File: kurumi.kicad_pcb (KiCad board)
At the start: 2 copper layers, 36 x 30 mm, 21 parts, among them J1 Power input, J2 LEDs, J3 Ext MOSFET/relay, U1 ESP32-C3_SUPERMINI, U2 SN74LVC1T45DRL, U3 TPS54308

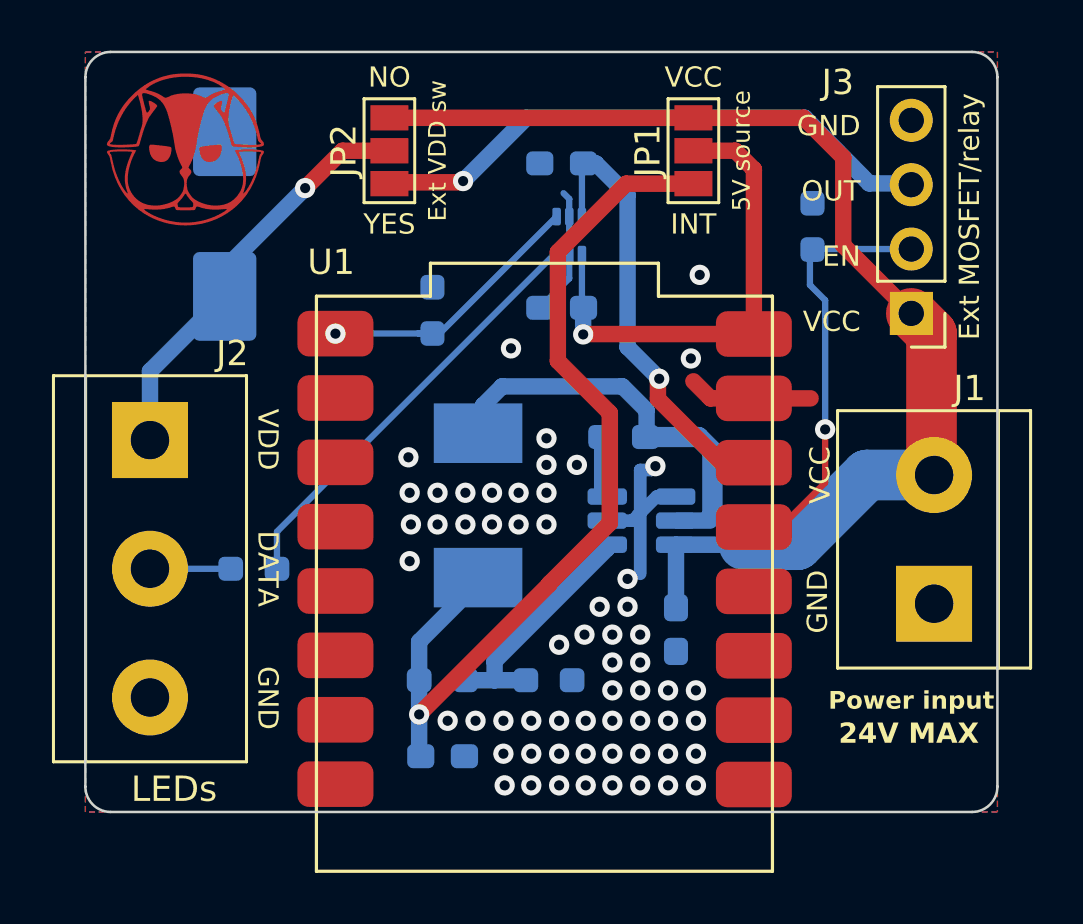
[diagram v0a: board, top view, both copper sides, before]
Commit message: Parts updates, BOM and CPL
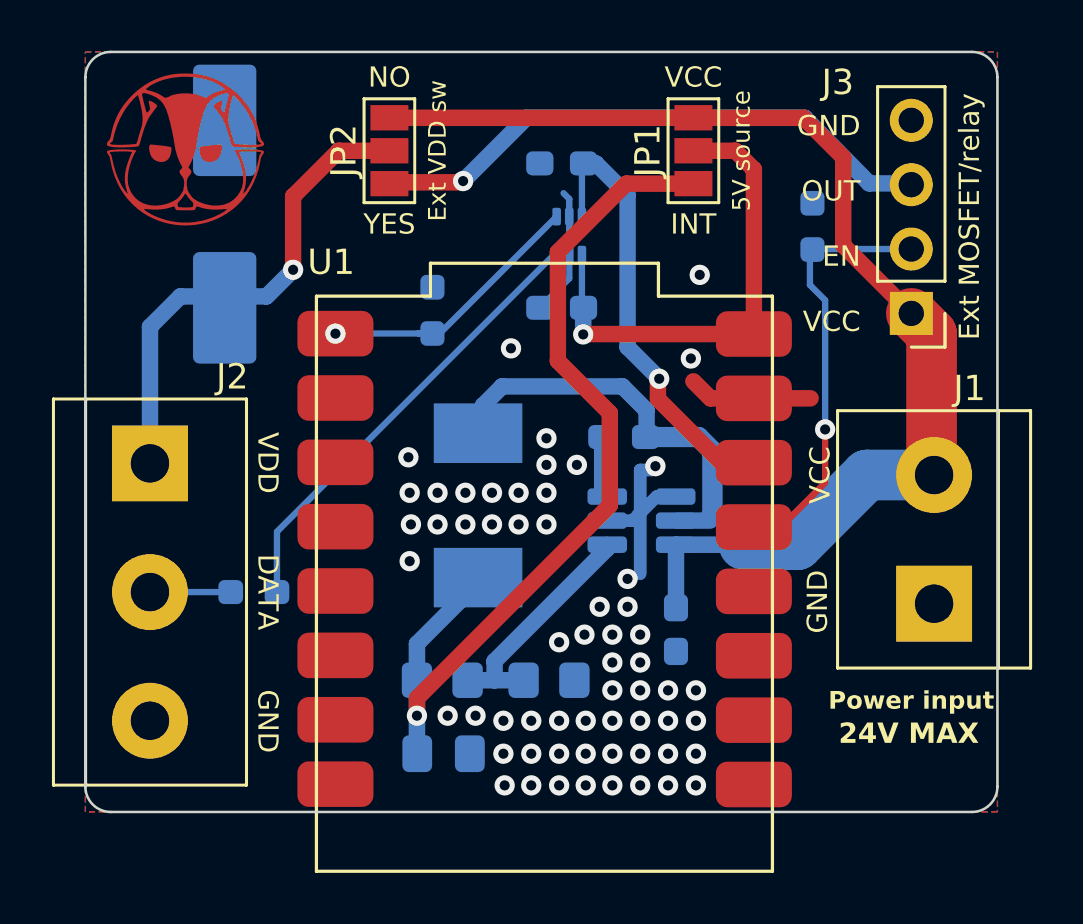
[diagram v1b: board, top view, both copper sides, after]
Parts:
- C5: footprint Capacitor_SMD:C_0603_1608Metric_Pad1.08x0.95mm_HandSolder -> Capacitor_SMD:C_0805_2012Metric_Pad1.18x1.45mm_HandSolder
- C6: footprint Capacitor_SMD:CP_Elec_8x10 -> Capacitor_SMD:CP_Elec_8x10.5
- R4: value 100k -> 100K; footprint Resistor_SMD:R_0603_1608Metric_Pad0.98x0.95mm_HandSolder -> Resistor_SMD:R_0805_2012Metric_Pad1.20x1.40mm_HandSolder
- R5: value 13.7k -> 13.7K; footprint Resistor_SMD:R_0603_1608Metric_Pad0.98x0.95mm_HandSolder -> Resistor_SMD:R_0805_2012Metric_Pad1.20x1.40mm_HandSolder
- moved R1 0.92 mm to (20.2, 33.4)
- moved J2 0.92 mm to (16.1, 28.3)
- moved C5 0.11 mm to (27.7, 39.8)
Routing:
- net VDD: track 16.4 -> 18.5 mm
- net Net-(U2-A): track 17.0 -> 18.0 mm
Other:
- board text removed: "LEDs"

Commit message: Minor changes
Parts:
- moved C4 0.95 mm to (35.8, 27.3)
- moved U3 0.45 mm to (35.1, 30.6)
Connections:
- U3 pad 5: GND -> unconnected-(U3-EN-Pad5)
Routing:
- net GND: track 19.3 -> 0.00 mm, vias 60 -> 75
- net +3.3V: track 17.8 -> 22.5 mm
- net V_OUT: track 37.0 -> 35.1 mm
- net VDD_EN: track 16.9 -> 18.8 mm
- net Net-(U3-BOOT): track 2.44 -> 3.15 mm
- net +5V: track 19.1 -> 18.5 mm
- net Net-(U3-SW): track 16.1 -> 15.4 mm, vias 0 -> 2

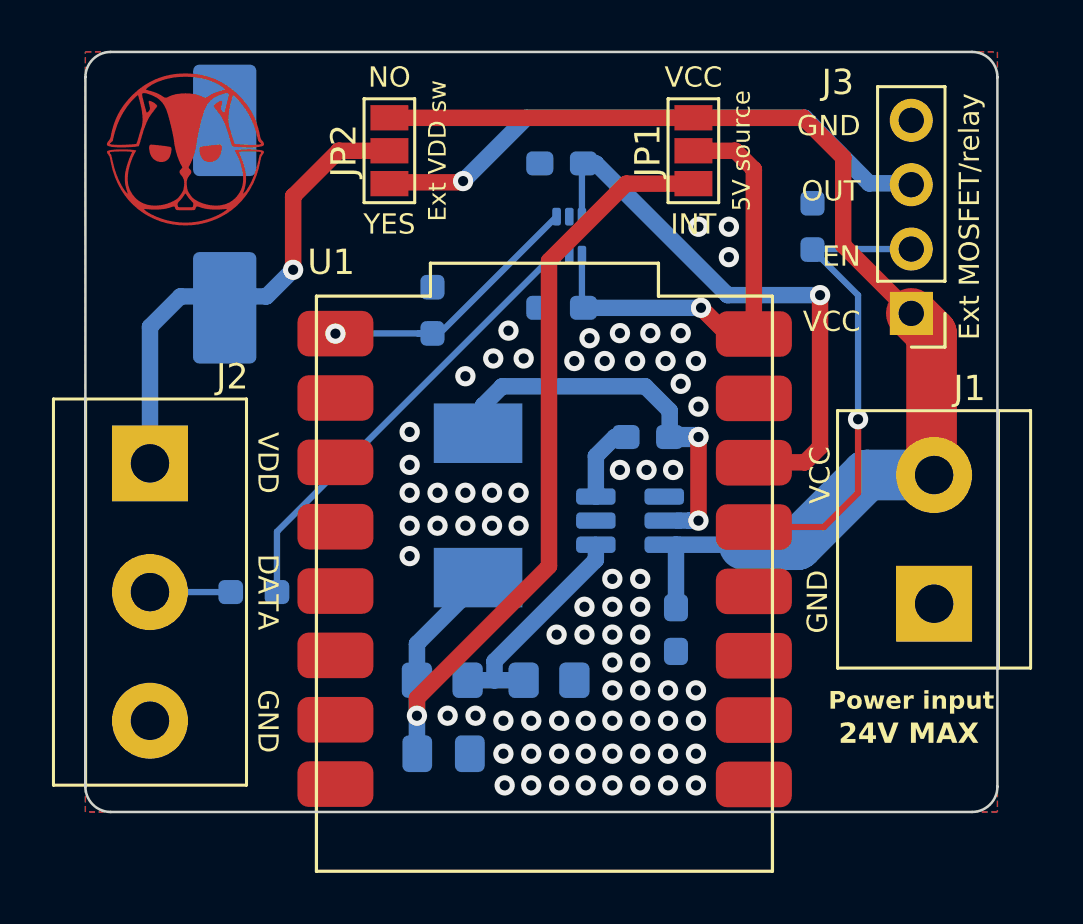
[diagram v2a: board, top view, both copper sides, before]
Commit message: Addes USB slot, fixed libraries
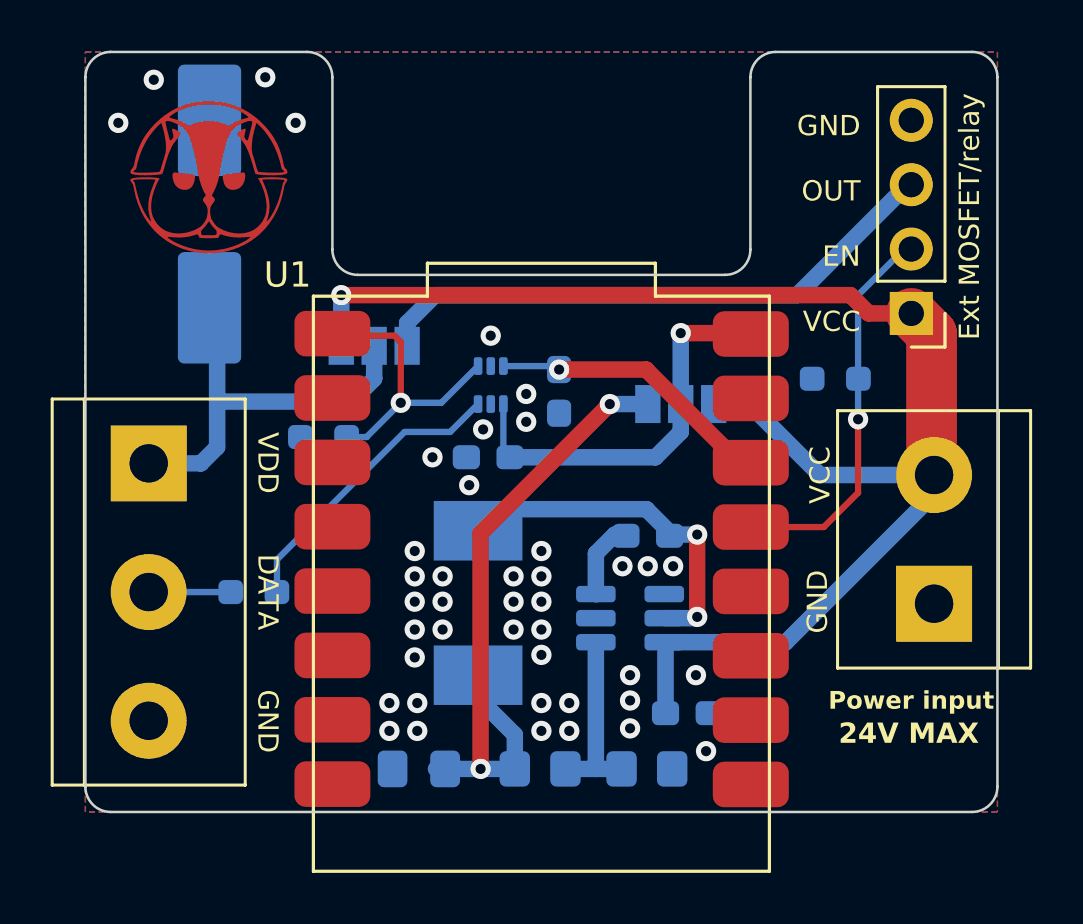
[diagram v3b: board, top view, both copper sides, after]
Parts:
- JP1, JP2: moved to B.Cu
- moved JP1 10.0 mm to (37.1, 26.0), turned to 0 degrees
- moved C2 9.00 mm to (32.3, 25.5), turned to 90 degrees
- moved JP2 7.72 mm to (25.0, 23.7), turned to 0 degrees
- moved U2 6.66 mm to (29.6, 25.2)
- moved R2 6.59 mm to (23.0, 27.3), turned to 180 degrees
- moved C1 6.57 mm to (29.5, 28.1)
- moved R3 6.08 mm to (43.2, 25.0), turned to 180 degrees
- moved R5 5.21 mm to (35.8, 40.4)
- moved R4 5.21 mm to (31.6, 40.4)
- moved C4 3.90 mm to (35.8, 31.2)
- moved L1 3.85 mm to (29.1, 33.9)
- moved U3 3.85 mm to (35.1, 34.5)
- moved C3 3.33 mm to (37.4, 38.2), turned to 0 degrees
- moved REF** 1.44 mm to (15.3, 14.0)
- moved C5 1.14 mm to (26.8, 40.4), turned to 180 degrees
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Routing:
- net VCC: track 45.0 -> 57.9 mm, vias 0 -> 1
- net +3.3V: track 22.5 -> 11.3 mm
- net V_OUT: track 35.1 -> 25.4 mm, vias 1 -> 2
- net Net-(U2-A): track 18.0 -> 11.8 mm
- net VDD_EN: track 18.8 -> 15.3 mm
- net +5V: track 18.5 -> 15.8 mm
- net Net-(U3-FB): track 9.39 -> 7.22 mm
- net Net-(U3-SW): track 15.4 -> 14.2 mm
- net VDD: track 18.5 -> 17.4 mm, vias 1 -> 0
- net V_SW: track 22.8 -> 22.5 mm, vias 1 -> 0
- net GND: vias 75 -> 42
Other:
- outline, holes or cut-outs redrawn

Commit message: Buck converter fix by @CRImier
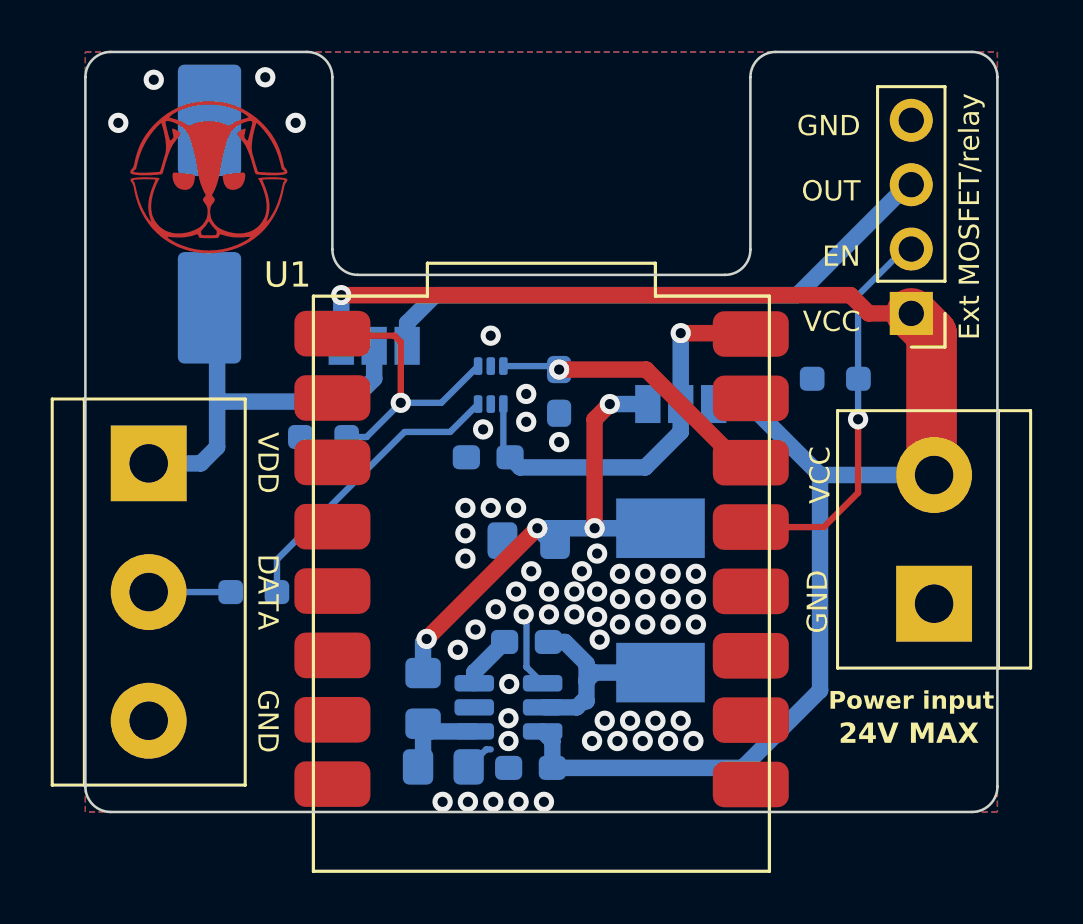
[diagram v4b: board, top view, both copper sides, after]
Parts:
- moved C5 10.00 mm to (31.1, 31.4)
- moved R5 8.03 mm to (27.7, 40.3)
- moved L1 7.20 mm to (36.3, 33.8), turned to 90 degrees
- moved C3 6.56 mm to (31.2, 40.4), turned to 180 degrees
- moved C4 6.36 mm to (31.0, 35.4)
- moved U3 5.95 mm to (30.3, 38.0)
- moved R4 5.39 mm to (26.9, 37.6), turned to -90 degrees
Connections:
- net Net-(U3-BOOT) renamed /BOOT
- net Net-(U3-FB) renamed /FB
- net Net-(U3-SW) renamed /SW
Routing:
- net VCC: track 57.9 -> 63.9 mm
- net /SW: track 14.2 -> 8.13 mm, vias 2 -> 0
- net V_OUT: track 25.4 -> 20.0 mm, vias 2 -> 4
- net GND: track 0.00 -> 3.92 mm, vias 42 -> 58
- net /FB: track 7.22 -> 3.88 mm
- net /BOOT: track 3.15 -> 2.13 mm

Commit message: Broken out 5V for relays and more
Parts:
- J3: value Ext MOSFET/relay -> Ext MOSFET/Relay; footprint Connector_PinHeader_2.54mm:PinHeader_1x04_P2.54mm_Vertical -> Connector_PinHeader_2.54mm:PinHeader_1x05_P2.54mm_Vertical
- moved J3 1.63 mm to (46.1, 24.1)
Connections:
- J3 pad 4: GND -> +5V
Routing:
- net +5V: track 16.1 -> 29.8 mm, vias 1 -> 2
- net VDD_EN: track 15.3 -> 13.5 mm
- net VCC: track 63.9 -> 62.4 mm
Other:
- board text added: "GND +5V OUT EN VCC"
- board text removed: "GND OUT EN VCC"
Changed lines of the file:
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@@
 		)
 	)
-	(footprint "Connector_PinHeader_2.54mm:PinHeader_1x04_P2.54mm_Vertical"
+	(footprint "Connector_PinHeader_2.54mm:PinHeader_1x05_P2.54mm_Vertical"
 		(layer "F.Cu")
-		(at 46.2 22.42 180)
-		(descr "Through hole straight pin header, 1x04, 2.54mm pitch, single row")
-		(tags "Through hole pin header THT 1x04 2.54mm single row")
+		(at 46.15 24.05 180)
+		(descr "Through hole straight pin header, 1x05, 2.54mm pitch, single row")
+		(tags "Through hole pin header THT 1x05 2.54mm single row")
 		(property "Reference" "J3"
 			(at 0 -2.33 180)
@@
 			)
 		)
-		(property "Value" "Ext MOSFET/relay"
-			(at 0 9.95 180)
+		(property "Value" "Ext MOSFET/Relay"
+			(at 0 12.49 180)
 			(layer "F.Fab")
 			(hide yes)
@@
 			)
 		)
-		(property "Footprint" "Connector_PinHeader_2.54mm:PinHeader_1x04_P2.54mm_Vertical"
+		(property "Footprint" "Connector_PinHeader_2.54mm:PinHeader_1x05_P2.54mm_Vertical"
 			(at 0 0 180)
 			(unlocked yes)
@@
 			)
 		)
-		(property "Description" ""
+		(property "Description" "Generic connector, single row, 01x05, script generated"
 			(at 0 0 180)
 			(unlocked yes)
@@
 		(sheetname "Root")
 		(sheetfile "kurumi.kicad_sch")
-		(attr through_hole exclude_from_pos_files exclude_from_bom)
+		(attr through_hole)
 		(fp_line
 			(start 1.33 1.27)
-			(end 1.33 8.95)
+			(end 1.33 11.49)
 			(stroke
 				(width 0.12)
@@
 		)
 		(fp_line
-			(start -1.33 8.95)
-			(end 1.33 8.95)
+			(start -1.33 11.49)
+			(end 1.33 11.49)
 			(stroke
 				(width 0.12)
@@
 		(fp_line
 			(start -1.33 1.27)
-			(end -1.33 8.95)
+			(end -1.33 11.49)
 			(stroke
 				(width 0.12)
@@
 		)
 		(fp_line
-			(start 1.8 9.4)
+			(start 1.8 11.95)
 			(end 1.8 -1.8)
 			(stroke
@@
 		)
 		(fp_line
-			(start -1.8 9.4)
-			(end 1.8 9.4)
+			(start -1.8 11.95)
+			(end 1.8 11.95)
 			(stroke
 				(width 0.05)
@@
 		(fp_line
 			(start -1.8 -1.8)
-			(end -1.8 9.4)
+			(end -1.8 11.95)
 			(stroke
 				(width 0.05)
@@
 		)
 		(fp_line
-			(start 1.27 8.89)
-			(end -1.27 8.89)
+			(start 1.27 11.43)
+			(end -1.27 11.43)
 			(stroke
 				(width 0.1)
@@
 		(fp_line
 			(start 1.27 -1.27)
-			(end 1.27 8.89)
+			(end 1.27 11.43)
 			(stroke
 				(width 0.1)
@@
 		)
 		(fp_line
-			(start -1.27 8.89)
+			(start -1.27 11.43)
 			(end -1.27 -0.635)
 			(stroke
@@
 		)
 		(fp_text user "${REFERENCE}"
-			(at 0 3.81 -90)
+			(at 0 5.08 -90)
 			(layer "F.Fab")
 			(effects
@@
 			(layers "*.Cu" "*.Mask")
 			(remove_unused_layers no)
-			(net 2 "GND")
+			(net 1 "+5V")
 			(pinfunction "Pin_4")
 			(pintype "passive")
 		)
-		(model "${KICAD8_3DMODEL_DIR}/Connector_PinHeader_2.54mm.3dshapes/PinHeader_1x04_P2.54mm_Vertical.wrl"
+		(pad "5" thru_hole oval
+			(at 0 10.16 180)
+			(size 1.7 1.7)
+			(drill 1)
+			(layers "*.Cu" "*.Mask")
+			(remove_unused_layers no)
+			(net 2 "GND")
+			(pinfunction "Pin_5")
+			(pintype "passive")
+		)
+		(model "${KICAD8_3DMODEL_DIR}/Connector_PinHeader_2.54mm.3dshapes/PinHeader_1x05_P2.54mm_Vertical.wrl"
 			(offset
 				(xyz 0 0 0)
@@
 		(sheetname "Root")
 		(sheetfile "kurumi.kicad_sch")
-		(attr through_hole exclude_from_pos_files exclude_from_bom)
+		(attr through_hole exclude_from_pos_files)
 		(fp_line
 			(start -9 11.35)
@@
 	)
 	(gr_text "5V source"
-		(at 37.1 24.1 180)
+		(at 37.1 24.1 0)
 		(layer "B.SilkS")
 		(effects
@@
 		)
 	)
-	(gr_text "GND\n\nOUT\n\nEN\n\nVCC"
-		(at 44.2 18.88 0)
+	(gr_text "GND\n\n+5V\n\nOUT\n\nEN\n\nVCC"
+		(at 44.5 18.9 0)
 		(layer "F.SilkS")
 		(effects
@@
 	)
 	(segment
+		(start 43.75 17.5)
+		(end 44.82 16.43)
+		(width 0.65)
+		(layer "F.Cu")
+		(net 1)
+	)
+	(segment
+		(start 43.75 20)
+		(end 43.75 17.5)
+		(width 0.65)
+		(layer "F.Cu")
+		(net 1)
+	)
+	(segment
+		(start 44.82 16.43)
+		(end 46.15 16.43)
+		(width 0.65)
+		(layer "F.Cu")
+		(net 1)
+	)
+	(segment
 		(start 37.1 23.2)
 		(end 39.953227 23.2)
@@
 	)
 	(via
+		(at 43.75 20)
+		(size 0.8)
+		(drill 0.4)
+		(layers "F.Cu" "B.Cu")
+		(net 1)
+	)
+	(via
 		(at 37.1 23.2)
 		(size 0.8)
@@
 	)
 	(segment
+		(start 41.05 23.2)
+		(end 37.1 23.2)
+		(width 0.65)
+		(layer "B.Cu")
+		(net 1)
+	)
+	(segment
+		(start 37.15 23.25)
+		(end 37.1 23.2)
+		(width 0.65)
+		(layer "B.Cu")
+		(net 1)
+	)
+	(segment
 		(start 37.1 26)
 		(end 37.1 23.2)
@@
 		(net 1)
 	)
+	(segment
+		(start 43.75 20.5)
+		(end 41.05 23.2)
+		(width 0.65)
+		(layer "B.Cu")
+		(net 1)
+	)
+	(segment
+		(start 43.75 20)
+		(end 43.75 20.5)
+		(width 0.65)
+		(layer "B.Cu")
+		(net 1)
+	)
 	(via
 		(at 29.8 34.1)
@@
 	(segment
 		(start 43.8 21.7)
-		(end 44.52 22.42)
+		(end 46.15 24.05)
 		(width 0.65)
 		(layer "F.Cu")
@@
 	)
 	(segment
-		(start 46.2 22.42)
-		(end 47 23.22)
-		(width 2)
+		(start 46.15 24.05)
+		(end 47.1 25)
+		(width 1)
 		(layer "F.Cu")
 		(net 4)
 	)
 	(segment
-		(start 44.52 22.42)
-		(end 46.2 22.42)
-		(width 0.65)
+		(start 47.1 25)
+		(end 47.1 28.8)
+		(width 1)
 		(layer "F.Cu")
 		(net 4)
 	)
 	(segment
-		(start 23.7 21.7)
+		(start 26.15 21.7)
 		(end 43.8 21.7)
 		(width 0.65)
@@
 		(net 4)
 	)
-	(segment
-		(start 47 28.7)
-		(end 47.1 28.8)
-		(width 2)
-		(layer "F.Cu")
-		(net 4)
-	)
-	(segment
-		(start 47 23.22)
-		(end 47 28.7)
-		(width 2)
-		(layer "F.Cu")
-		(net 4)
-	)
 	(via
-		(at 23.7 21.7)
+		(at 26.15 21.7)
 		(size 0.8)
 		(drill 0.4)
@@
 	)
 	(segment
+		(start 26.15 21.7)
+		(end 24.55 21.7)
+		(width 0.65)
+		(layer "B.Cu")
+		(net 4)
+	)
+	(segment
 		(start 32.032501 39.302501)
 		(end 32.032501 40.36)
@@
 	)
 	(segment
-		(start 23.7 21.7)
-		(end 23.7 23.5)
+		(start 24.55 21.7)
+		(end 23.7 22.55)
 		(width 0.65)
 		(layer "B.Cu")
@@
 	)
 	(segment
+		(start 23.7 22.55)
+		(end 23.7 23.5)
+		(width 0.65)
+		(layer "B.Cu")
+		(net 4)
+	)
+	(segment
 		(start 39.8 26)
 		(end 38.4 26)
@@
 	)
 	(segment
-		(start 33.7 30.9)
-		(end 33.7 26.6)
-		(width 0.65)
-		(layer "F.Cu")
-		(net 6)
-	)
-	(segment
 		(start 31.44 30.9)
 		(end 27.07 35.27)
@@
 	)
 	(segment
-		(start 33.7 26.6)
-		(end 34.3 26)
+		(start 33.7 27.4)
+		(end 33.7 30.9)
 		(width 0.65)
 		(layer "F.Cu")
@@
 	)
 	(via
-		(at 34.3 26)
+		(at 33.7 27.4)
 		(size 0.8)
 		(drill 0.4)
@@
 	)
 	(segment
-		(start 34.3 26)
+		(start 34.7 26)
 		(end 35.8 26)
 		(width 0.65)
@@
 	)
 	(segment
+		(start 33.7 27)
+		(end 34.7 26)
+		(width 0.65)
+		(layer "B.Cu")
+		(net 6)
+	)
+	(segment
 		(start 31.93 31.39)
 		(end 32.1375 31.39)
@@
 	)
 	(segment
+		(start 33.7 27.4)
+		(end 33.7 27)
+		(width 0.65)
+		(layer "B.Cu")
+		(net 6)
+	)
+	(segment
 		(start 18.8 22.5)
 		(end 18.5 22.2)
@@
 	)
 	(segment
-		(start 44.1 21.7)
-		(end 45.92 19.88)
+		(start 44.1 23.56)
+		(end 46.15 21.51)
 		(width 0.25)
 		(layer "B.Cu")
@@
 	)
 	(segment
-		(start 45.92 19.88)
-		(end 46.2 19.88)
+		(start 44.1 26.6)
+		(end 44.1 23.56)
 		(width 0.25)
 		(layer "B.Cu")
@@
 	)
 	(segment
-		(start 44.1 26.6)
-		(end 44.1 21.7)
-		(width 0.25)
+		(start 39.8 21.7)
+		(end 29.35 21.7)
+		(width 0.65)
 		(layer "B.Cu")
-		(net 9)
+		(net 10)
 	)
 	(segment
-		(start 46.06 17.34)
-		(end 41.7 21.7)
+		(start 29.35 21.7)
+		(end 27.35 23.7)
 		(width 0.65)
 		(layer "B.Cu")
@@
 	)
 	(segment
-		(start 46.2 17.34)
-		(end 46.06 17.34)
+		(start 27.35 23.7)
+		(end 26.3 23.7)
 		(width 0.65)
 		(layer "B.Cu")
@@
 	)
 	(segment
-		(start 27.4 21.7)
-		(end 26.3 22.8)
+		(start 46.15 18.97)
+		(end 45.68 18.5)
 		(width 0.65)
 		(layer "B.Cu")
@@
 	)
 	(segment
-		(start 26.3 22.8)
-		(end 26.3 23.181625)
+		(start 45.68 18.5)
+		(end 43 18.5)
 		(width 0.65)
 		(layer "B.Cu")
@@
 	)
 	(segment
-		(start 41.7 21.7)
-		(end 27.4 21.7)
+		(start 43 18.5)
+		(end 39.8 21.7)
 		(width 0.65)
 		(layer "B.Cu")
